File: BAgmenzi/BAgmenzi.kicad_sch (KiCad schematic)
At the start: 0 parts

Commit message: added libraries, other changes in sch, started pcb
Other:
- sheet NRF ports: added PPG_I2C{SCL, SDA}; removed none
- sheet PPG ports: added PPG_I2C{SCL, SDA}; removed PPG_SCL, PPG_SDA
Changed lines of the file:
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@@
 	)
 	(sheet
-		(at 22.86 78.74)
-		(size 48.26 22.86)
+		(at 29.21 72.39)
+		(size 35.56 48.26)
 		(exclude_from_sim no)
 		(in_bom yes)
@@
 		)
 		(property "Sheetname" "NRF"
-			(at 22.86 78.0284 0)
+			(at 29.21 71.6784 0)
 			(effects
 				(font
@@
 		)
 		(property "Sheetfile" "nrf.kicad_sch"
-			(at 22.86 102.1846 0)
+			(at 29.21 121.2346 0)
 			(effects
 				(font
@@
 					(size 1.27 1.27)
 				)
+			)
+		)
+		(pin "PPG_I2C{SCL, SDA}" bidirectional
+			(at 55.88 120.65 270)
+			(effects
+				(font
+					(size 1.27 1.27)
+				)
+				(justify left)
 			)
 		)
@@
 		)
 		(pin "PPG_GPIO" input
-			(at 64.77 151.13 90)
+			(at 35.56 151.13 90)
 			(effects
 				(font
@@
 		)
 		(pin "PPG_INT" input
-			(at 59.69 151.13 90)
-			(effects
-				(font
-					(size 1.27 1.27)
-				)
-				(justify right)
-			)
-		)
-		(pin "PPG_SCL" output
-			(at 34.29 151.13 90)
-			(effects
-				(font
-					(size 1.27 1.27)
-				)
-				(justify right)
-			)
-		)
-		(pin "PPG_SDA" output
-			(at 38.1 151.13 90)
+			(at 39.37 151.13 90)
 			(effects
 				(font
@@
 		)
 		(pin "SPARE_PIN" input
-			(at 54.61 151.13 90)
+			(at 43.18 151.13 90)
 			(effects
 				(font
+					(size 1.27 1.27)
+				)
+				(justify right)
+			)
+		)
+		(pin "PPG_I2C{SCL, SDA}" bidirectional
+			(at 57.15 151.13 90)
+			(effects
+				(font

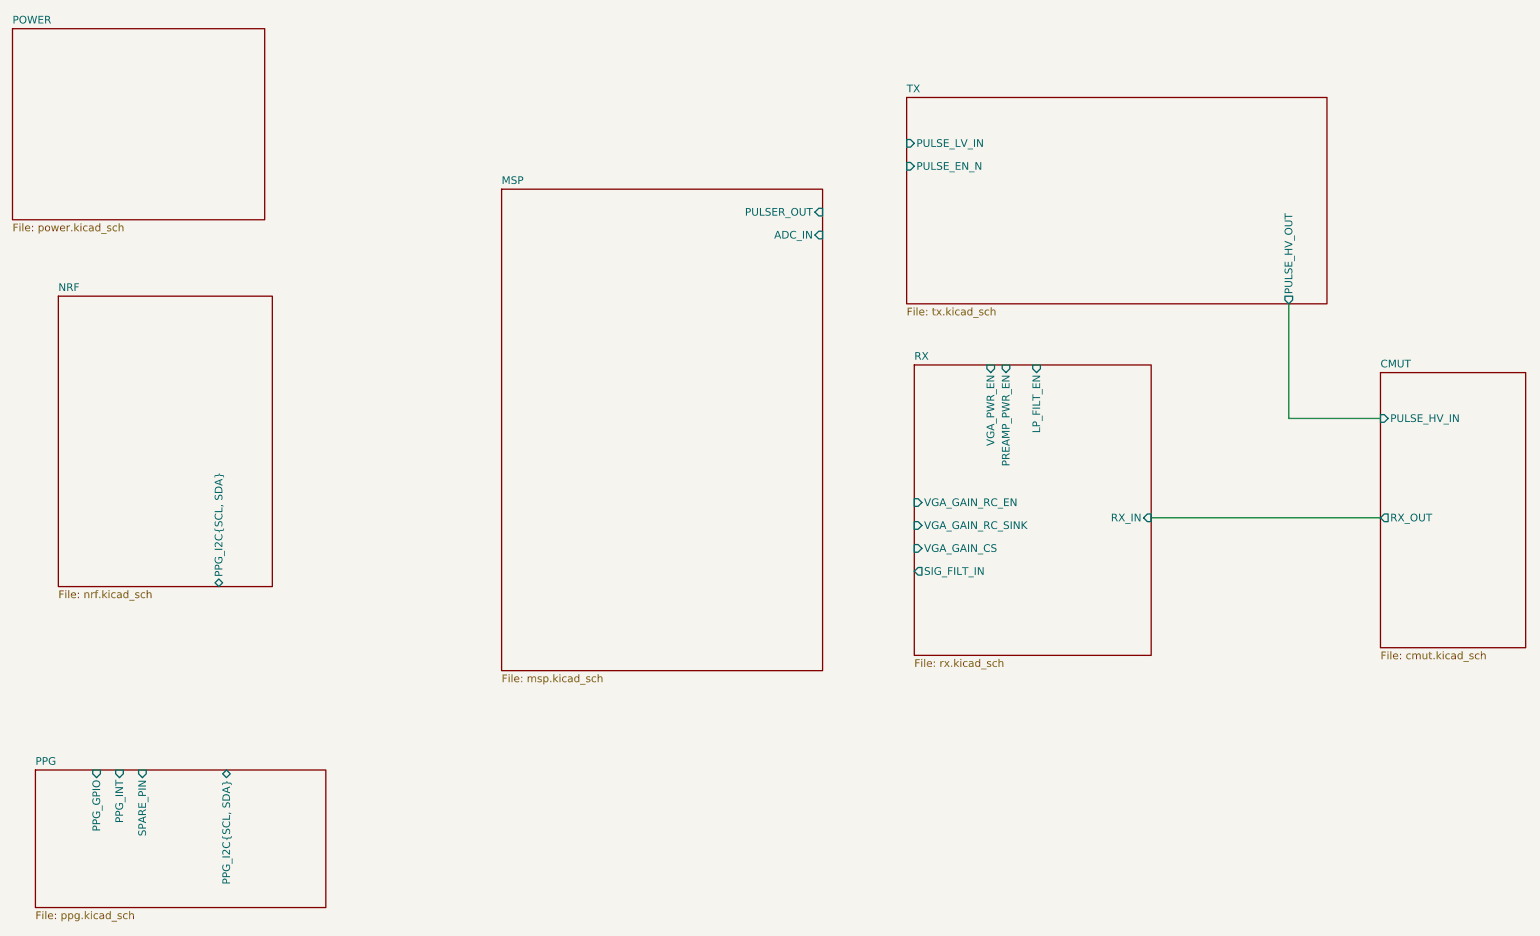
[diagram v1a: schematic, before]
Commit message: changed VRX rail and deleted U12
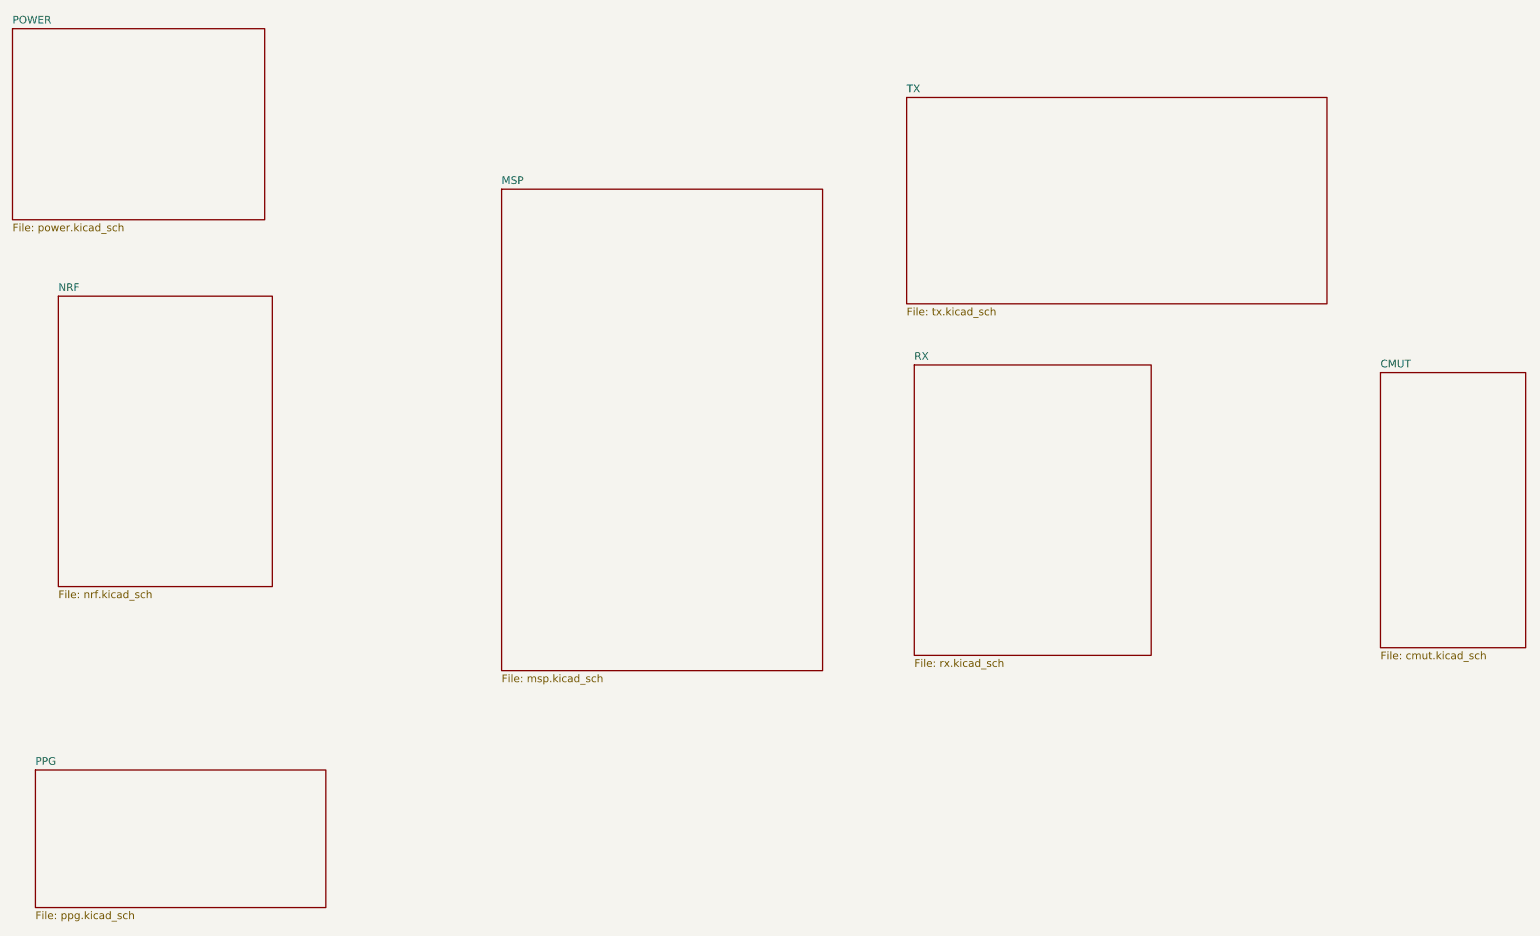
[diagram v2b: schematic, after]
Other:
- sheet CMUT ports: added none; removed PULSE_HV_IN, RX_OUT
- sheet MSP ports: added none; removed ADC_IN, PULSER_OUT
- sheet NRF ports: added none; removed PPG_I2C{SCL, SDA}
- sheet PPG ports: added none; removed PPG_GPIO, PPG_I2C{SCL, SDA}, PPG_INT, SPARE_PIN
- sheet RX ports: added none; removed LP_FILT_EN, PREAMP_PWR_EN, RX_IN, SIG_FILT_IN, VGA_GAIN_CS, VGA_GAIN_RC_EN, VGA_GAIN_RC_SINK, VGA_PWR_EN
- sheet TX ports: added none; removed PULSE_EN_N, PULSE_HV_OUT, PULSE_LV_IN
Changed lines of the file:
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@@
 	(generator_version "9.0")
 	(paper "A4")
-	(wire
-		(pts
-			(xy 210.82 109.22) (xy 248.92 109.22)
-		)
-		(stroke
-			(width 0)
-			(type default)
-		)
-	)
-	(wire
-		(pts
-			(xy 233.68 73.66) (xy 233.68 92.71)
-		)
-		(stroke
-			(width 0)
-			(type default)
-		)
-	)
-	(wire
-		(pts
-			(xy 233.68 92.71) (xy 248.92 92.71)
-		)
-		(stroke
-			(width 0)
-			(type default)
-		)
-	)
 	(sheet
 		(at 102.87 54.61)
@@
 			)
 		)
-		(pin "PULSER_OUT" input
-			(at 156.21 58.42 0)
-			(effects
-				(font
-					(size 1.27 1.27)
-				)
-				(justify right)
-			)
-		)
-		(pin "ADC_IN" input
-			(at 156.21 62.23 0)
-			(effects
-				(font
-					(size 1.27 1.27)
-				)
-				(justify right)
-			)
-		)
 		(instances
 			(project "BAgmenzi"
@@
 			)
 		)
-		(pin "PULSE_HV_OUT" output
-			(at 233.68 73.66 270)
-			(effects
-				(font
-					(size 1.27 1.27)
-				)
-				(justify left)
-			)
-		)
-		(pin "PULSE_LV_IN" input
-			(at 170.18 46.99 180)
-			(effects
-				(font
-					(size 1.27 1.27)
-				)
-				(justify left)
-			)
-		)
-		(pin "PULSE_EN_N" input
-			(at 170.18 50.8 180)
-			(effects
-				(font
-					(size 1.27 1.27)
-				)
-				(justify left)
-			)
-		)
 		(instances
 			(project "BAgmenzi"
@@
 			)
 		)
-		(pin "LP_FILT_EN" input
-			(at 191.77 83.82 90)
-			(effects
-				(font
-					(size 1.27 1.27)
-				)
-				(justify right)
-			)
-		)
-		(pin "RX_IN" input
-			(at 210.82 109.22 0)
-			(effects
-				(font
-					(size 1.27 1.27)
-				)
-				(justify right)
-			)
-		)
-		(pin "SIG_FILT_IN" output
-			(at 171.45 118.11 180)
-			(effects
-				(font
-					(size 1.27 1.27)
-				)
-				(justify left)
-			)
-		)
-		(pin "VGA_PWR_EN" input
-			(at 184.15 83.82 90)
-			(effects
-				(font
-					(size 1.27 1.27)
-				)
-				(justify right)
-			)
-		)
-		(pin "PREAMP_PWR_EN" input
-			(at 186.69 83.82 90)
-			(effects
-				(font
-					(size 1.27 1.27)
-				)
-				(justify right)
-			)
-		)
-		(pin "VGA_GAIN_CS" input
-			(at 171.45 114.3 180)
-			(effects
-				(font
-					(size 1.27 1.27)
-				)
-				(justify left)
-			)
-		)
-		(pin "VGA_GAIN_RC_SINK" input
-			(at 171.45 110.49 180)
-			(effects
-				(font
-					(size 1.27 1.27)
-				)
-				(justify left)
-			)
-		)
-		(pin "VGA_GAIN_RC_EN" input
-			(at 171.45 106.68 180)
-			(effects
-				(font
-					(size 1.27 1.27)
-				)
-				(justify left)
-			)
-		)
 		(instances
 			(project "BAgmenzi"
@@
 			)
 		)
-		(pin "PPG_I2C{SCL, SDA}" bidirectional
-			(at 55.88 120.65 270)
-			(effects
-				(font
-					(size 1.27 1.27)
-				)
-				(justify left)
-			)
-		)
 		(instances
 			(project "BAgmenzi"
@@
 			)
 		)
-		(pin "PPG_GPIO" input
-			(at 35.56 151.13 90)
-			(effects
-				(font
-					(size 1.27 1.27)
-				)
-				(justify right)
-			)
-		)
-		(pin "PPG_INT" input
-			(at 39.37 151.13 90)
-			(effects
-				(font
-					(size 1.27 1.27)
-				)
-				(justify right)
-			)
-		)
-		(pin "SPARE_PIN" input
-			(at 43.18 151.13 90)
-			(effects
-				(font
-					(size 1.27 1.27)
-				)
-				(justify right)
-			)
-		)
-		(pin "PPG_I2C{SCL, SDA}" bidirectional
-			(at 57.15 151.13 90)
-			(effects
-				(font
-					(size 1.27 1.27)
-				)
-				(justify right)
-			)
-		)
 		(instances
 			(project "BAgmenzi"
@@
 			)
 		)
-		(pin "PULSE_HV_IN" input
-			(at 248.92 92.71 180)
-			(effects
-				(font
-					(size 1.27 1.27)
-				)
-				(justify left)
-			)
-		)
-		(pin "RX_OUT" output
-			(at 248.92 109.22 180)
-			(effects
-				(font
-					(size 1.27 1.27)
-				)
-				(justify left)
-			)
-		)
